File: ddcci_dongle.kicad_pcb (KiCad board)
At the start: 4 copper layers, 30.1 x 50.7 mm, 52 parts, among them U1 PCA9306, U10 TPD1E05U06DPY, U11 TPD1E05U06DPY, U12 TPD1E05U06DPY, U3 RP2040, U4 W25Q16JVUXIQ, U6 TPD1E05U06DPY, U8 TPD1E05U06DPY, U9 TPD1E05U06DPY, Y1 ABM8-272-T3

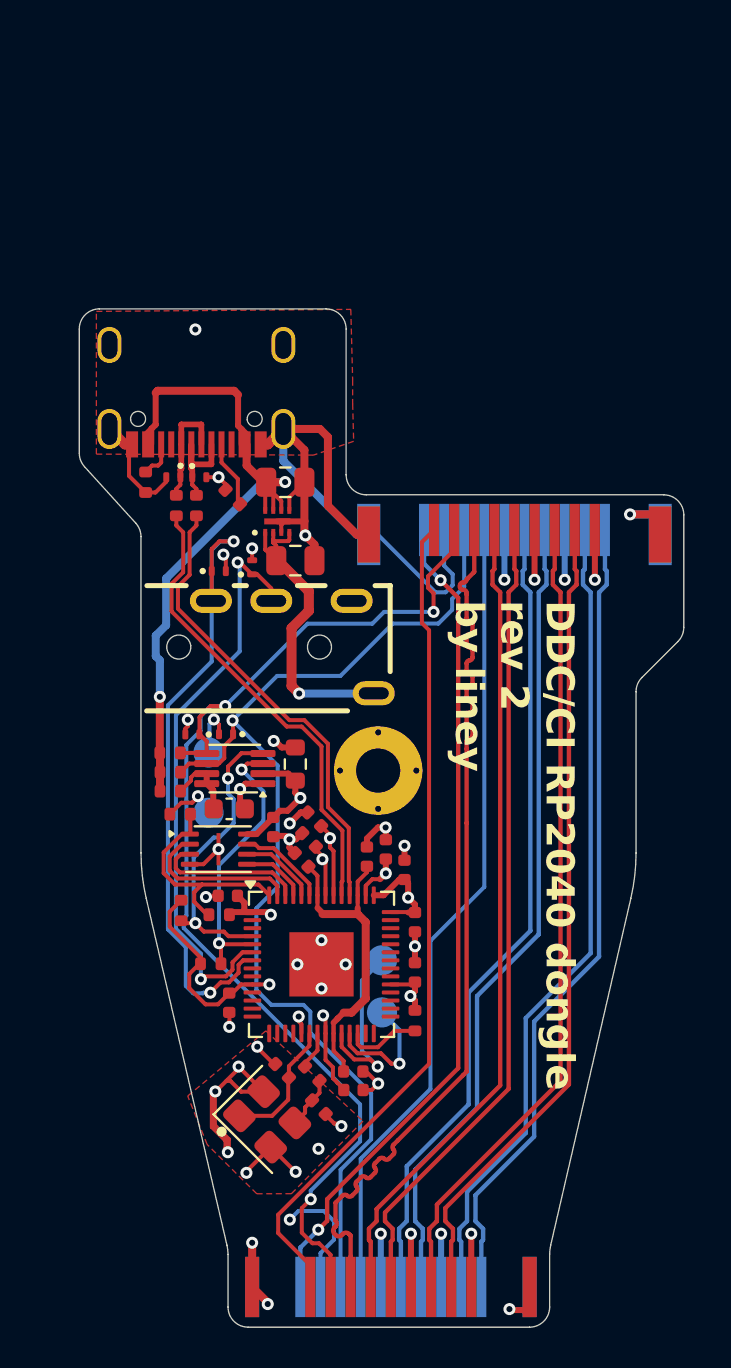
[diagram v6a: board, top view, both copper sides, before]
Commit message: Change pinout of the TRRS jack
This way the board won't burn if a TRS cable is plugged in.

Signed-off-by: Elvira Khabirova <lineprinter0@gmail.com>
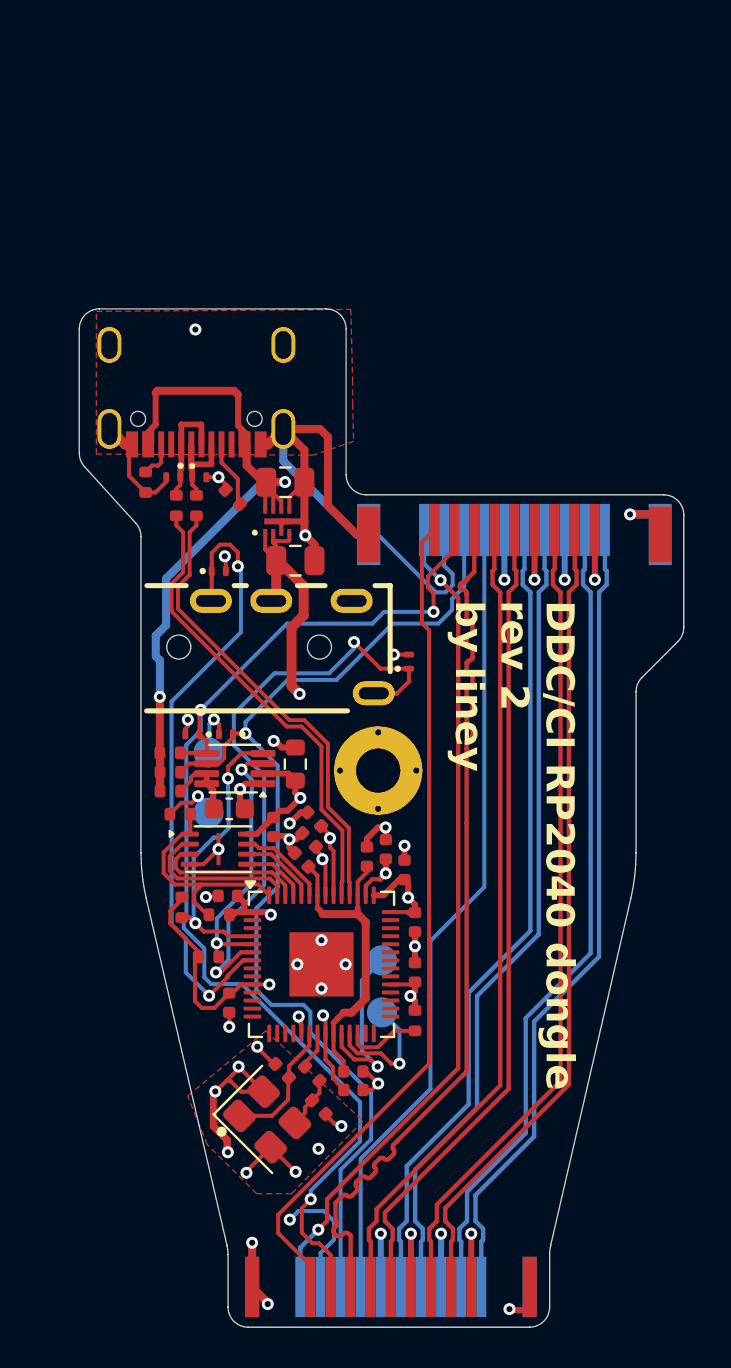
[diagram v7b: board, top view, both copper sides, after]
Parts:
- moved U10 9.10 mm to (129.0, 104.2)
- moved R14 0.36 mm to (119.0, 118.9)
- moved R13 0.16 mm to (117.7, 116.5)
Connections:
- CN1 pad A: +3V3 -> /PERIPHERAL_SDA
- CN1 pad C: /PERIPHERAL_SDA -> +3V3
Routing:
- net +3V3: track 56.4 -> 54.6 mm
- net /PERIPHERAL_SDA: track 28.8 -> 30.3 mm
- net /PERIPHERAL_SCK: track 32.5 -> 31.3 mm
- net /DISPLAY_SCK: track 55.4 -> 54.4 mm
- net /SHIFTED_DISPLAY_SCK: track 13.9 -> 13.3 mm
